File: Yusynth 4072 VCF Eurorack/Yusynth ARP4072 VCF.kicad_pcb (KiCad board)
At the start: 2 copper layers, 78 parts, among them J1 Audio In 1, J2 Audio In 2, J3 V/Oct, J4 CV 1, J5 CV 2, J6 Audio In 1, J7 CONN_02X05, Q1 MMDT3906, Q2 MMDT3906, Q3 MMDT3906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

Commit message: Fixed LM3900 pin mapping. File cleanup
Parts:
- removed RV1 - In 1: 47Ka, Potentiometers:Potentiometer_Alps_RK09L_Sleve_Single_Horizontal
- removed RV2 - In 2: 47Ka, Potentiometers:Potentiometer_Alps_RK09L_Sleve_Single_Horizontal
- removed RV3 - Freq: 47Kb, Potentiometers:Potentiometer_Alps_RK09L_Sleve_Single_Horizontal
- removed RV4 - CV 1: 47Kb, Potentiometers:Potentiometer_Alps_RK09L_Sleve_Single_Horizontal
- removed RV5 - CV 2: 47Kb, Potentiometers:Potentiometer_Alps_RK09L_Sleve_Single_Horizontal
- removed RV6 - Res: 100Kb, Potentiometers:Potentiometer_Alps_RK09L_Double_Horizontal
- added R44: 22K, Resistors_SMD:R_0603, F.Cu at (163.8, 69.8)
- added RV1: 47Ka, Potentiometers:Potentiometer_Alps_RK09L_Sleve_Single_Horizontal, B.Cu at (188.0, 116.8)
- added RV2: 47Ka, Potentiometers:Potentiometer_Alps_RK09L_Sleve_Single_Horizontal, B.Cu at (166.4, 116.8)
- added RV3: 47Kb, Potentiometers:Potentiometer_Alps_RK09L_Sleve_Single_Horizontal, B.Cu at (188.0, 62.2)
- added RV4: 47Kb, Potentiometers:Potentiometer_Alps_RK09L_Sleve_Single_Horizontal, B.Cu at (188.0, 88.9)
- added RV5: 47Kb, Potentiometers:Potentiometer_Alps_RK09L_Sleve_Single_Horizontal, B.Cu at (166.4, 88.9)
- added RV6: Resonance 100K, Potentiometers:Potentiometer_Alps_RK09L_Double_Horizontal, B.Cu at (166.4, 62.2)
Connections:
- U2 pad 1: Net-(C1-Pad2) -> Net-(Q2-Pad6)
- U2 pad 11: Net-(Q6-Pad6) -> Net-(C10-Pad2)
- U2 pad 12: Net-(C10-Pad2) -> Net-(Q6-Pad6)
- U2 pad 13: Net-(C9-Pad2) -> Net-(Q5-Pad6)
- U2 pad 14: Earth -> +12V
- U2 pad 2: Net-(C4-Pad2) -> Net-(Q4-Pad6)
- U2 pad 3: Net-(Q4-Pad6) -> Net-(C4-Pad2)
- U2 pad 6: Net-(Q2-Pad6) -> Net-(C1-Pad2)
- U2 pad 7: -12V -> Earth
- U2 pad 8: Net-(Q5-Pad6) -> Net-(C9-Pad2)

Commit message: Changed dual-gang pot to single gang for easier sourcing. Rotated pot footprints
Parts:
- RV6: value Resonance 100K -> 47Ka; footprint Potentiometers:Potentiometer_Alps_RK09L_Double_Horizontal -> Potentiometers:Potentiometer_Alps_RK09L_Sleve_Single_Horizontal
- moved RV2 12.5 mm to (161.3, 128.3), turned to 90 degrees
- moved RV1 12.5 mm to (182.9, 128.3), turned to 90 degrees
- moved RV5 10.8 mm to (161.3, 98.4), turned to 90 degrees
- moved RV4 10.8 mm to (183.0, 98.4), turned to 90 degrees
- moved RV3 9.67 mm to (182.9, 70.5), turned to 90 degrees
- moved RV6 9.67 mm to (161.3, 70.5), turned to 90 degrees
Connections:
- U2 pad 14: +12V -> Earth
- U2 pad 7: Earth -> -12V

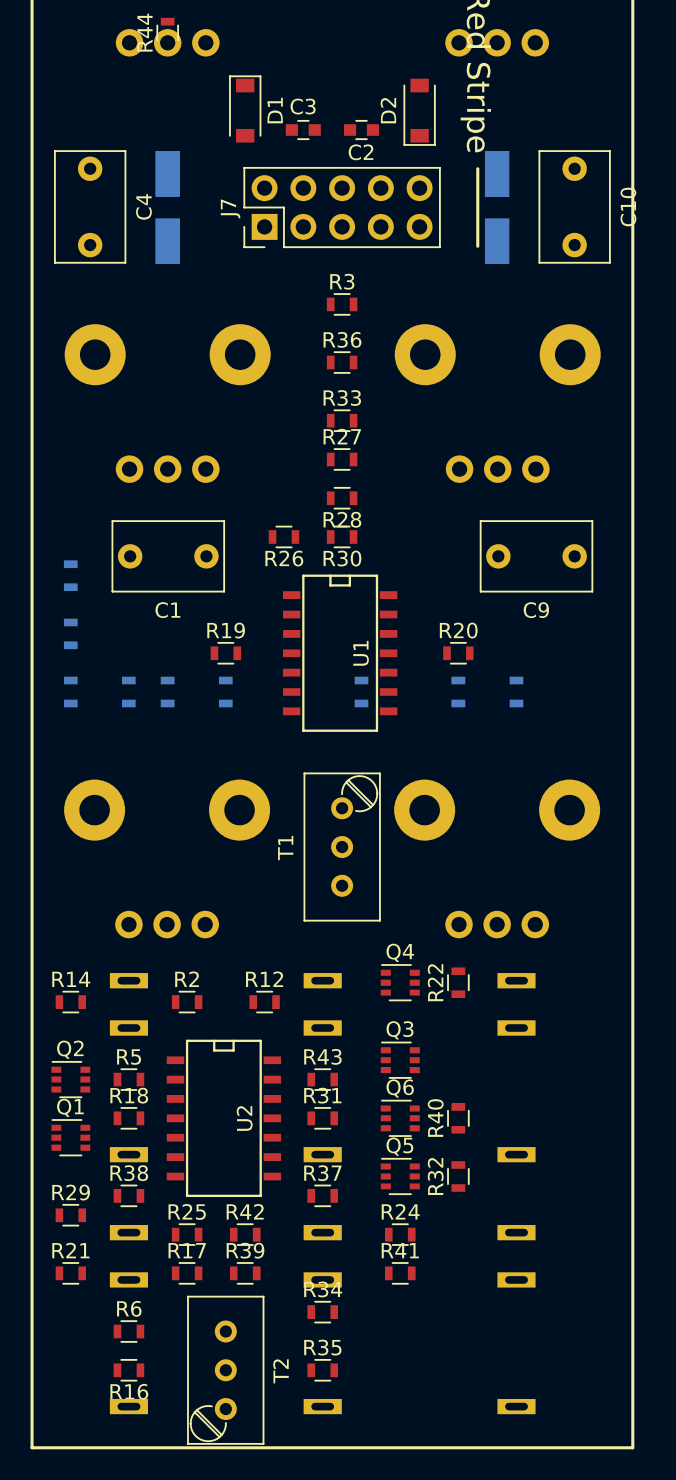
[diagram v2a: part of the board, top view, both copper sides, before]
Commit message: Repositioned components for better grouping
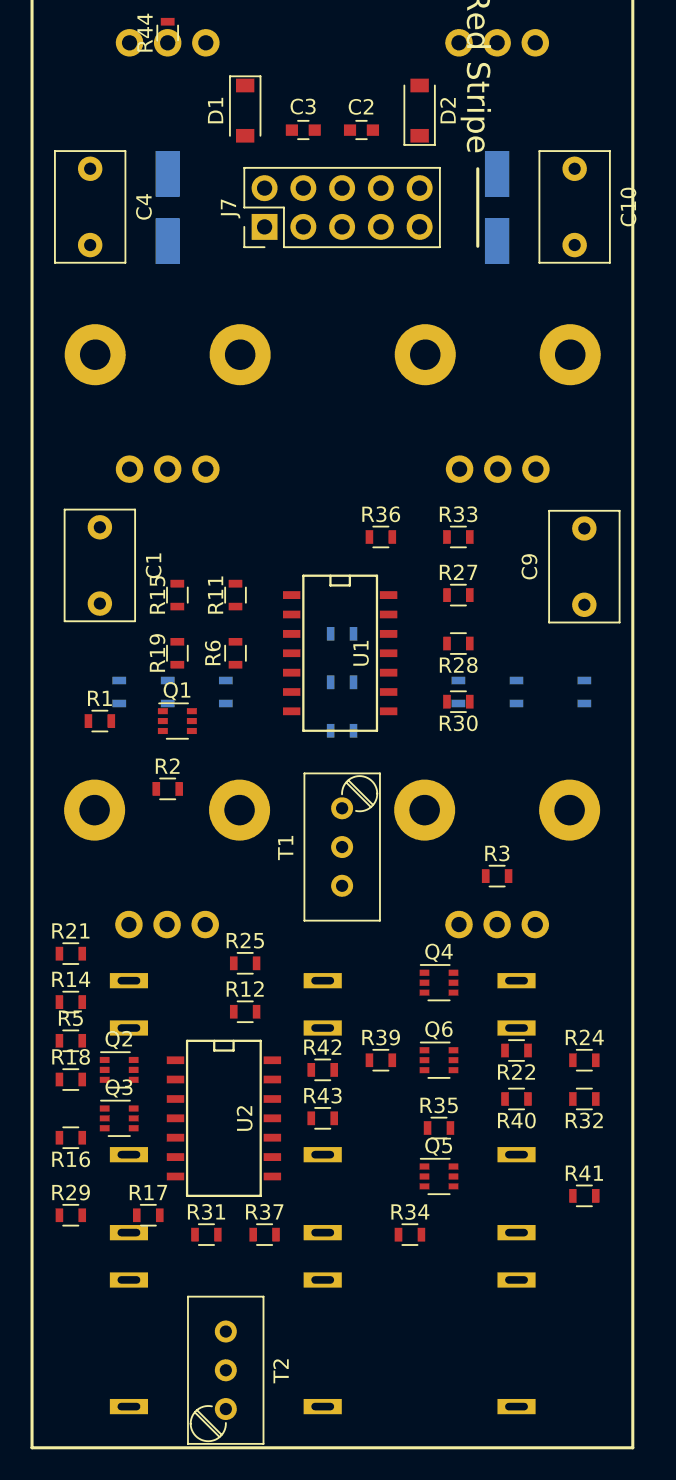
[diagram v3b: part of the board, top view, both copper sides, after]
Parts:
- R1, R11, R15: moved to F.Cu
- R20, R26, R38: moved to B.Cu
- moved R6 45.0 mm to (168.3, 110.5), turned to 90 degrees
- moved R38 44.5 mm to (191.1, 113.0), turned to 90 degrees
- moved R3 38.8 mm to (185.4, 125.1)
- moved Q1 28.2 mm to (164.5, 114.9)
- moved R21 21.0 mm to (157.5, 130.2)
- moved Q3 18.8 mm to (160.7, 141.0)
- moved R25 18.2 mm to (168.9, 130.8)
- moved R35 17.6 mm to (181.6, 141.6)
- moved R24 16.6 mm to (191.1, 137.2)
- moved R39 16.6 mm to (177.8, 137.2)
- moved R16 15.7 mm to (157.5, 142.2)
- moved R2 14.0 mm to (163.8, 119.4)
- moved R26 13.3 mm to (175.3, 115.6)
- moved R30 13.2 mm to (182.9, 113.7)
- moved R41 13.1 mm to (191.1, 146.1)
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
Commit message: Trace updates
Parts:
- moved R44 34.5 mm to (174.0, 102.9), turned to 180 degrees
- moved R17 1.80 mm to (161.3, 146.1)
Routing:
- net -12V: track 0.00 -> 190.8 mm, vias 0 -> 5
- net +12V: track 0.00 -> 163.1 mm, vias 0 -> 3
- net Net-(C4-Pad2): track 0.00 -> 94.0 mm, vias 0 -> 4
- net Net-(C4-Pad1): track 0.00 -> 90.5 mm
- net Net-(C10-Pad1): track 0.00 -> 76.6 mm, vias 0 -> 2
- net Net-(C10-Pad2): track 0.00 -> 73.4 mm, vias 0 -> 4
- net Net-(C9-Pad2): track 0.00 -> 66.2 mm, vias 0 -> 2
- net Net-(R12-Pad2): track 0.00 -> 64.4 mm, vias 0 -> 7
- net Net-(J6-Pad1): track 0.00 -> 63.1 mm, vias 0 -> 1
- net Net-(Q1-Pad2): track 0.00 -> 62.3 mm
- net Net-(J5-Pad1): track 0.00 -> 60.9 mm, vias 0 -> 1
- net Net-(J4-Pad1): track 0.00 -> 56.8 mm
- net Net-(C1-Pad1): track 0.00 -> 51.3 mm, vias 0 -> 2
- net Net-(Q4-Pad2): track 0.00 -> 51.3 mm, vias 0 -> 3
- net Net-(R7-Pad2): track 0.00 -> 50.9 mm, vias 0 -> 1
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- added copper zone on B.Cu, net Earth
- added copper zone on F.Cu, net Earth

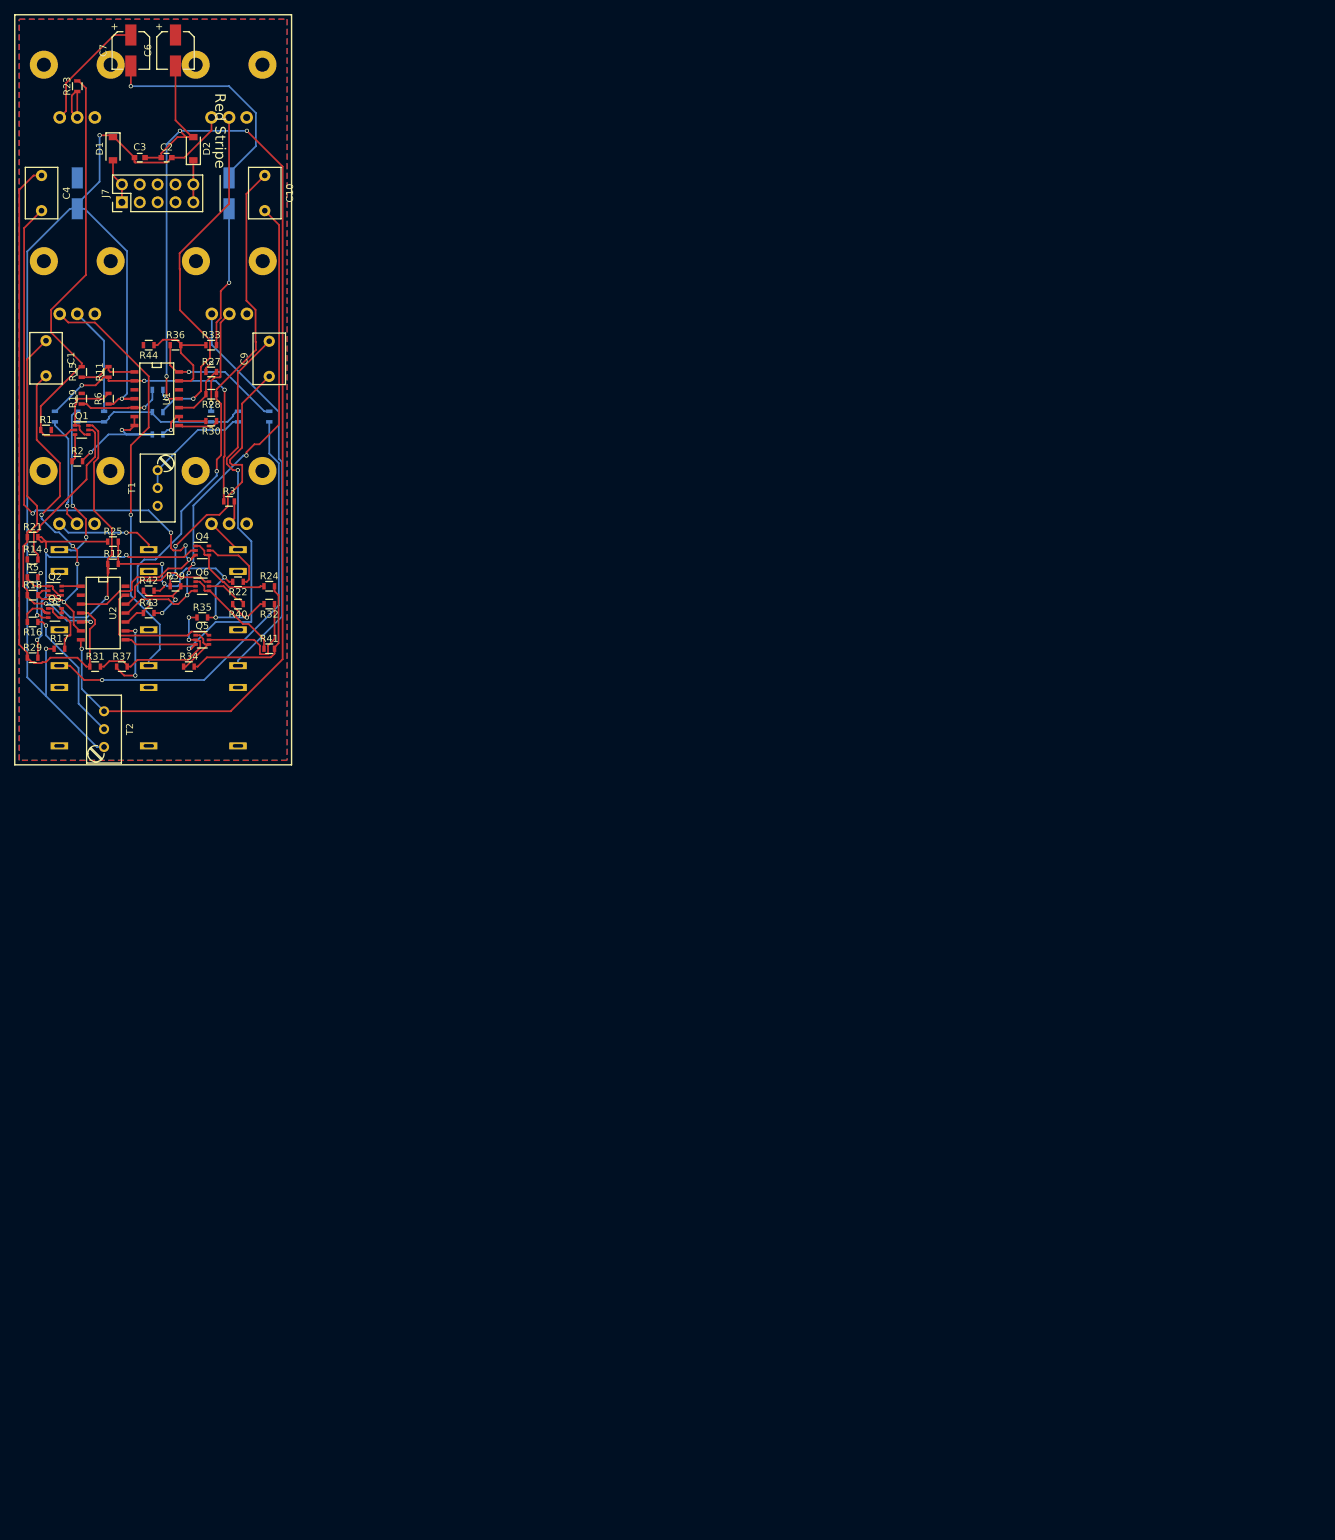
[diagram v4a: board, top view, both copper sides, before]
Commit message: Finished tracks and vias with no DRC errors.
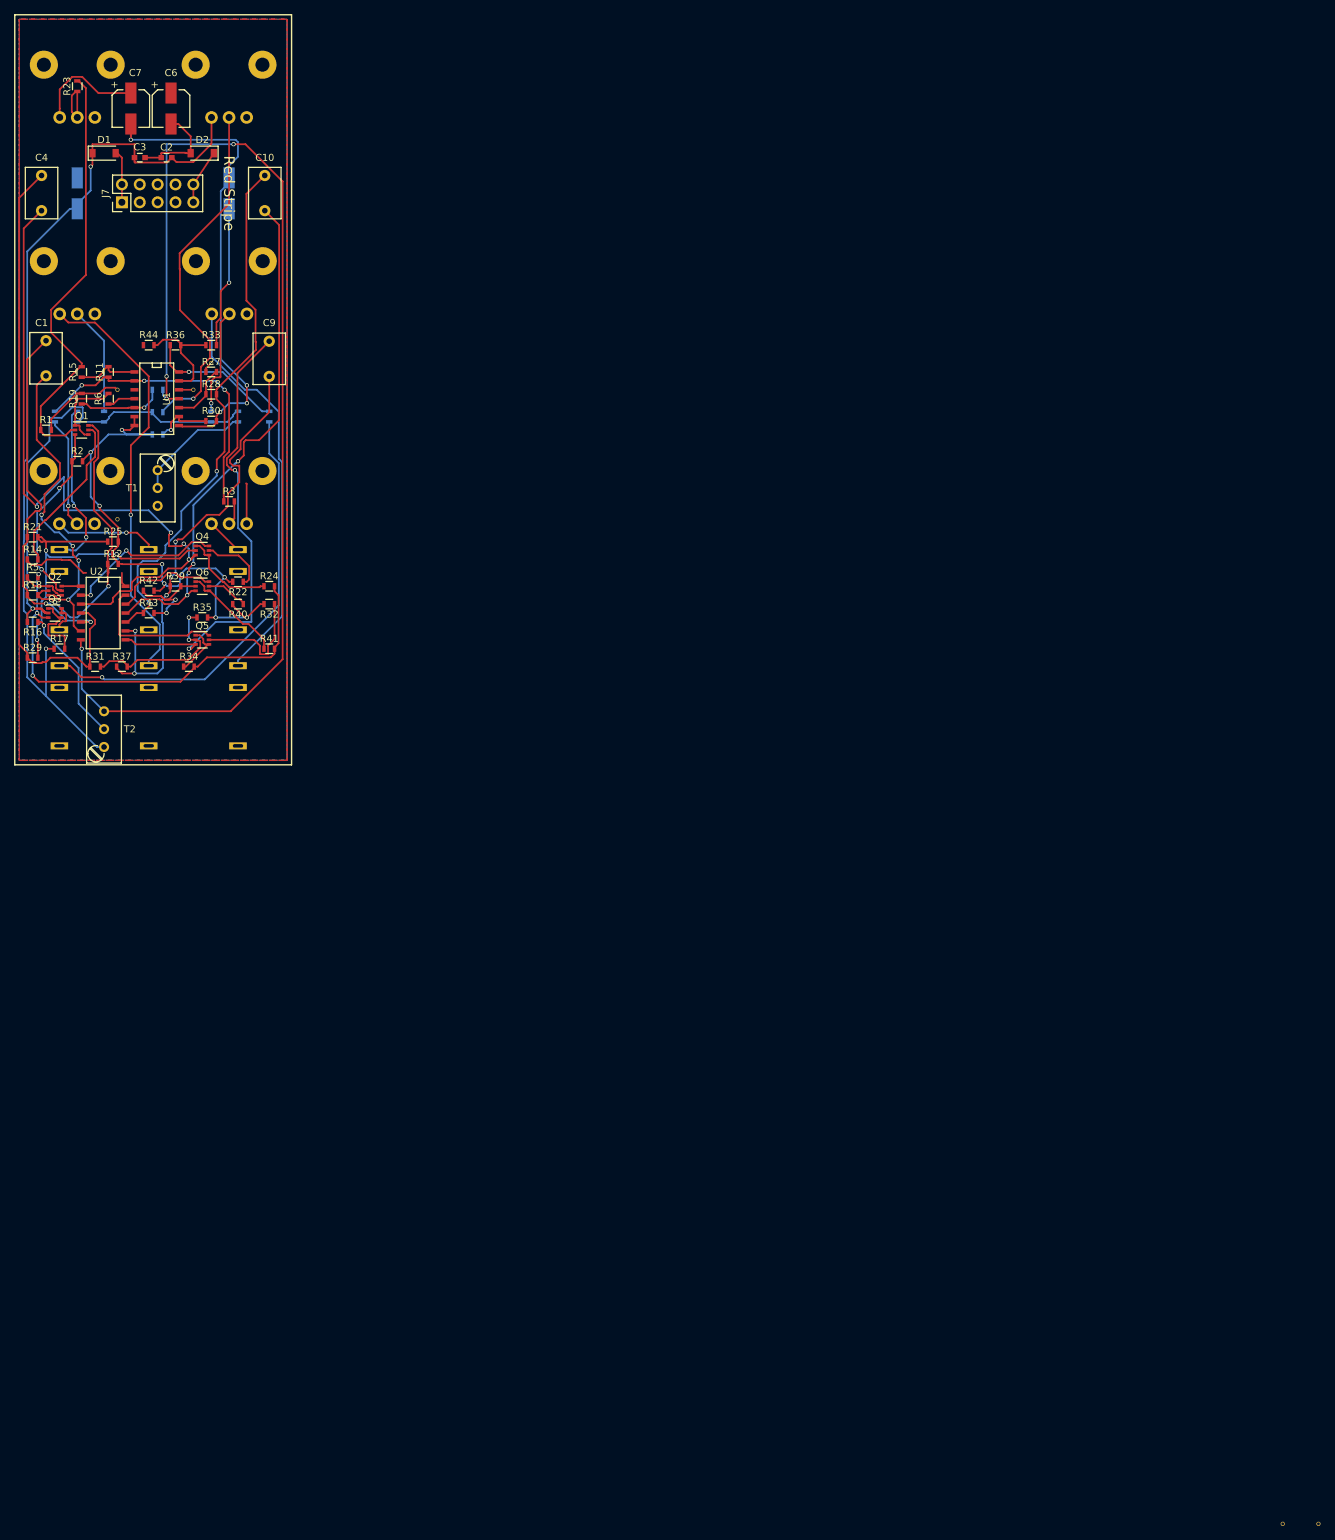
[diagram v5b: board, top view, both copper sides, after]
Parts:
- added REF**: VIA-0.6mm, YusynthLib:VIA-0.6mm, F.Cu at (165.1, 135.3)
- added REF**: VIA-0.6mm, YusynthLib:VIA-0.6mm, F.Cu at (169.5, 109.2)
- added REF**: VIA-0.6mm, YusynthLib:VIA-0.6mm, F.Cu at (169.5, 127.6)
- added REF**: VIA-0.6mm, YusynthLib:VIA-0.6mm, F.Cu at (170.2, 135.3)
- added REF**: VIA-0.6mm, YusynthLib:VIA-0.6mm, F.Cu at (180.3, 109.2)
- added REF**: VIA-0.6mm, YusynthLib:VIA-0.6mm, F.Cu at (182.9, 105.4)
- moved C6 8.28 mm to (177.2, 69.2)
- moved C7 8.26 mm to (171.4, 69.2)
- moved D1 1.42 mm to (167.6, 75.6), turned to 0 degrees
- moved D2 1.42 mm to (181.6, 75.6), turned to 180 degrees
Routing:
- net Net-(Q3-Pad2): track 31.2 -> 69.5 mm, vias 0 -> 1
- net Earth: track 2.95 -> 39.0 mm, vias 1 -> 0
- net Net-(C7-Pad2): track 38.9 -> 71.7 mm, vias 1 -> 4
- net Net-(Q3-Pad3): track 31.0 -> 63.8 mm, vias 2 -> 3
- net +12V: track 163.1 -> 132.5 mm, vias 3 -> 2
- net Net-(Q1-Pad3): track 3.98 -> 27.3 mm, vias 0 -> 2
- net Net-(Q4-Pad6): track 0.00 -> 22.9 mm, vias 0 -> 2
- net Net-(C9-Pad1): track 50.1 -> 65.8 mm, vias 4 -> 5
- net Net-(R12-Pad2): track 64.4 -> 79.4 mm, vias 7 -> 8
- net -12V: track 190.8 -> 180.2 mm, vias 5 -> 4
- net Net-(C4-Pad2): track 94.0 -> 99.5 mm
- net Net-(Q3-Pad1): track 8.48 -> 11.2 mm
- net Net-(D2-Pad1): track 5.97 -> 7.86 mm
- net Net-(C7-Pad1): track 17.3 -> 15.8 mm
- net Net-(Q6-Pad2): track 16.6 -> 15.4 mm
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
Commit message: Minor text tweaks
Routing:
- net Net-(R23-Pad1): track 7.50 -> 3.90 mm
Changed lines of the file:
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@@
     (thickness 1.6)
     (drawings 5)
-    (tracks 926)
+    (tracks 924)
     (zones 0)
     (modules 85)
@@
   (layers
     (0 F.Cu signal)
-    (31 B.Cu signal)
+    (31 B.Cu signal hide)
     (32 B.Adhes user)
     (33 F.Adhes user)
@@
     (47 F.CrtYd user)
     (48 B.Fab user)
-    (49 F.Fab user hide)
+    (49 F.Fab user)
   )
   (setup
@@
     (pad_to_mask_clearance 0.2)
     (aux_axis_origin 0 0)
-    (visible_elements FFFEFFFF)
+    (visible_elements FFFF7B3F)
     (pcbplotparams
       (layerselection 0x00030_80000001)
@@
     (tags "resistor 0603")
     (attr smd)
-    (fp_text reference R11 (at 0 1.27 270) (layer F.SilkS)
+    (fp_text reference R11 (at 0 1.47 270) (layer F.SilkS)
       (effects (font (size 1 1) (thickness 0.15)))
     )
@@
     (tags "resistor 0603")
     (attr smd)
-    (fp_text reference R15 (at 0 1.27 270) (layer F.SilkS)
+    (fp_text reference R15 (at 0 1.47 270) (layer F.SilkS)
       (effects (font (size 1 1) (thickness 0.15)))
     )
@@
     (tags "resistor 0603")
     (attr smd)
-    (fp_text reference R19 (at 0 1.27 270) (layer F.SilkS)
+    (fp_text reference R19 (at 0 1.47 270) (layer F.SilkS)
       (effects (font (size 1 1) (thickness 0.15)))
     )
@@
     (descr "Spindle Trimmer Potentiometer, Bourns 3296W, https://www.bourns.com/pdfs/3296.pdf")
     (tags "Spindle Trimmer Potentiometer   Bourns 3296W")
-    (fp_text reference T1 (at -2.54 -3.66 180) (layer F.SilkS)
+    (fp_text reference T1 (at 3.175 -1.905 180) (layer F.SilkS)
       (effects (font (size 1 1) (thickness 0.15)))
     )
-    (fp_text value 2.2K (at -2.54 3.67 90) (layer F.Fab)
+    (fp_text value 2.2K (at 3.175 1.27 180) (layer F.Fab)
       (effects (font (size 1 1) (thickness 0.15)))
     )
@@
     (descr "Spindle Trimmer Potentiometer, Bourns 3296W, https://www.bourns.com/pdfs/3296.pdf")
     (tags "Spindle Trimmer Potentiometer   Bourns 3296W")
-    (fp_text reference T2 (at -2.54 -3.66 360) (layer F.SilkS)
+    (fp_text reference T2 (at -8.255 1.905 360) (layer F.SilkS)
       (effects (font (size 1 1) (thickness 0.15)))
     )
-    (fp_text value 47K (at -2.54 3.67 270) (layer F.Fab)
+    (fp_text value 47K (at -8.255 -1.27 360) (layer F.Fab)
       (effects (font (size 1 1) (thickness 0.15)))
     )
@@
     (tags "CMS SOJ")
     (attr smd)
-    (fp_text reference U1 (at 0 -1.27 270) (layer F.SilkS)
+    (fp_text reference U1 (at -5.08 1.27 360) (layer F.SilkS)
       (effects (font (size 1 1) (thickness 0.15)))
     )
@@
   (segment (start 186.750003 132.775001) (end 183.830001 132.775001) (width 0.25) (layer F.Cu) (net 46))
   (segment (start 183.135 132.08) (end 182.56 132.08) (width 0.25) (layer F.Cu) (net 46) (status 20))
-  (segment (start 163.83 66.79) (end 163.83 70.485) (width 0.25) (layer F.Cu) (net 47) (status 30))
+  (segment (start 163.83 70.485) (end 163.83 69.212208) (width 0.25) (layer F.Cu) (net 47))
+  (segment (start 163.83 69.212208) (end 163.83 66.79) (width 0.25) (layer F.Cu) (net 47))
   (segment (start 163.83 66.79) (end 163.63 66.79) (width 0.25) (layer F.Cu) (net 47) (status 30))
-  (segment (start 163.63 66.79) (end 163.054999 67.365001) (width 0.25) (layer F.Cu) (net 47) (status 10))
-  (segment (start 163.054999 67.365001) (end 163.054999 69.709999) (width 0.25) (layer F.Cu) (net 47))
-  (segment (start 163.054999 69.709999) (end 163.369999 70.024999) (width 0.25) (layer F.Cu) (net 47) (status 20))
   (segment (start 182.56 134.590002) (end 182.56 132.73) (width 0.25) (layer F.Cu) (net 48) (status 20))
   (segment (start 184.644999 136.515001) (end 184.484999 136.515001) (width 0.25) (layer F.Cu) (net 48))
